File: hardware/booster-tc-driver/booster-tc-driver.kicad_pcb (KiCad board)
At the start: 2 copper layers, 53.5 x 89 mm, 42 parts, among them J1 62201021121, J2 EHT-105-01-S-D, Q1 T2N7002AK, U1 STM32F405RGTx, U2 LT1963AxST-3.3, U4 IF-D95T << must be T, U6 IF-D95T << must be T

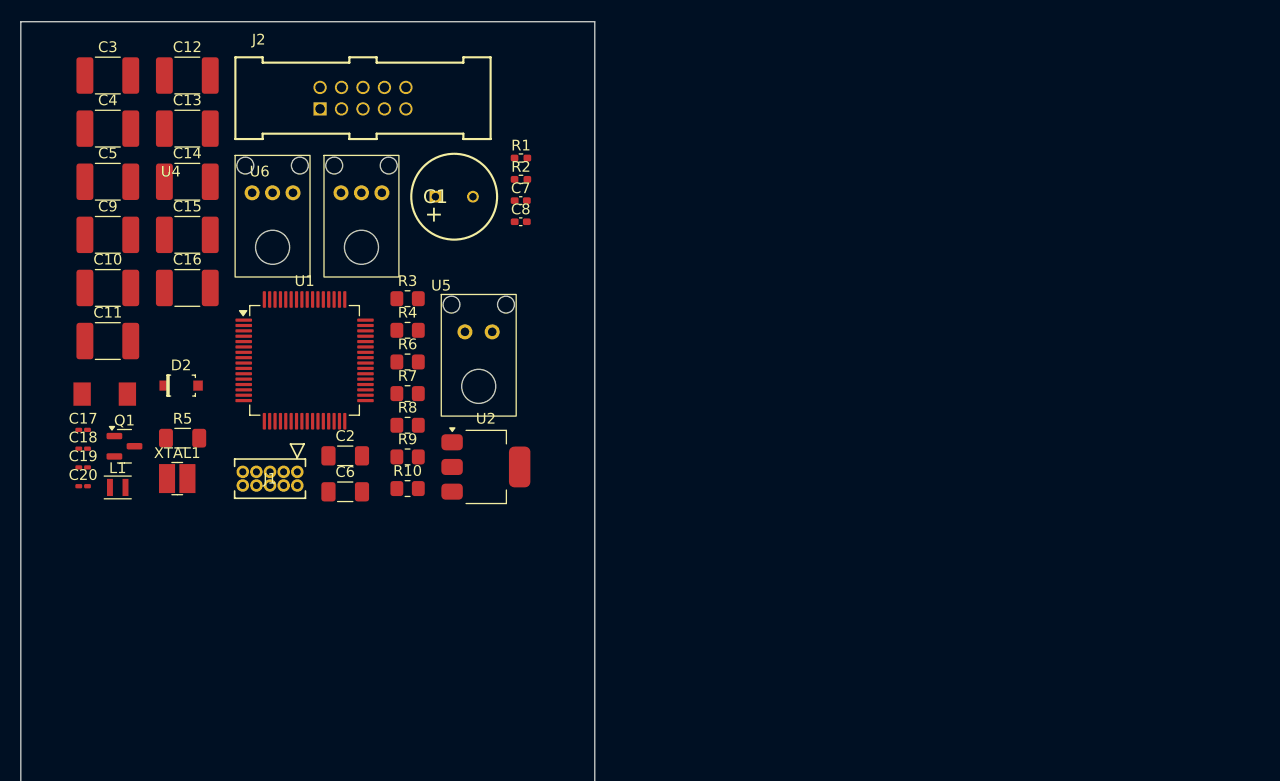
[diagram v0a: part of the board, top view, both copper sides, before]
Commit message: pin assignments
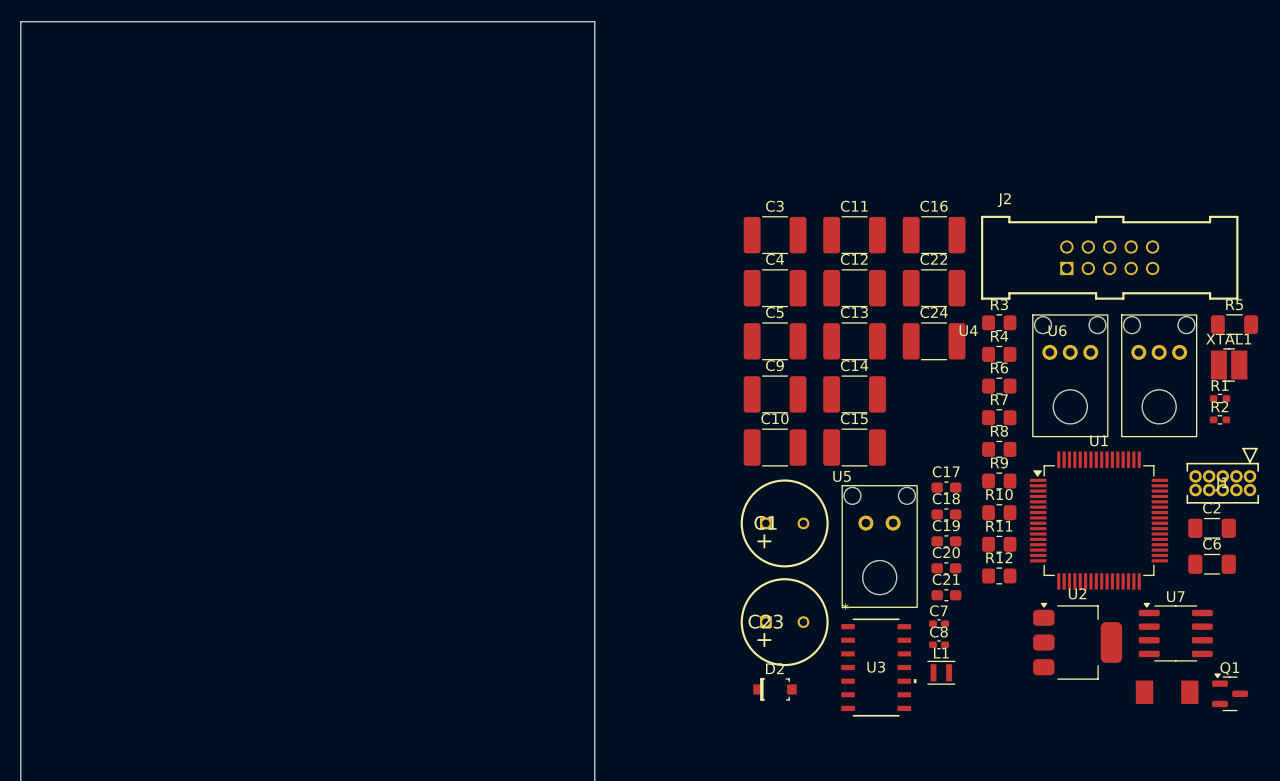
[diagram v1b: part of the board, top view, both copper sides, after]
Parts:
- added C21: 1n CGA3EAC0G2A102J080AA, Capacitor_SMD:C_0603_1608Metric_Pad1.08x0.95mm_HandSolder, F.Cu at (160.8, 112.5)
- added C22: 1u 885012210031, Capacitor_SMD:C_1812_4532Metric_Pad1.57x3.40mm_HandSolder, F.Cu at (159.6, 83.8)
- added C23: 860020474014, Library:CAPPRD350W52D800H1300, F.Cu at (143.9, 115.0)
- added C24: 1u 885012210031, Capacitor_SMD:C_1812_4532Metric_Pad1.57x3.40mm_HandSolder, F.Cu at (159.6, 88.8)
- added R11: 1k MCU0805MD1051BP500, Resistor_SMD:R_0805_2012Metric_Pad1.20x1.40mm_HandSolder, F.Cu at (165.7, 107.7)
- added R12: 1k MCU0805MD1051BP500, Resistor_SMD:R_0805_2012Metric_Pad1.20x1.40mm_HandSolder, F.Cu at (165.7, 110.7)
- added U3: MAX9202ESD+, Library:21-0041B_14-L, F.Cu at (154.2, 119.2)
- added U7: TC7662Bx0A, Package_SO:SOIC-8_3.9x4.9mm_P1.27mm, F.Cu at (182.2, 116.0)
- C17, C18, C19, C20: footprint Capacitor_SMD:C_0201_0603Metric_Pad0.64x0.40mm_HandSolder -> Capacitor_SMD:C_0603_1608Metric_Pad1.08x0.95mm_HandSolder
- moved Q1 105.6 mm to (187.2, 121.6)
- moved D1 102.9 mm to (181.4, 121.5)
- moved R5 98.6 mm to (187.6, 87.2)
- moved XTAL1 98.6 mm to (187.1, 91.0)
- moved J1 88.8 mm to (189.1, 101.4)
- moved C2 81.1 mm to (185.5, 106.2)
- moved C6 81.1 mm to (185.5, 109.6)
- moved C20 80.8 mm to (160.8, 110.0)
- moved C19 80.8 mm to (160.8, 107.4)
- moved C18 80.7 mm to (160.8, 104.9)
- moved C17 80.6 mm to (160.8, 102.4)
- moved L1 78.7 mm to (160.3, 119.7)
- moved U4 75.8 mm to (168.8, 86.3)
- moved U6 75.8 mm to (177.1, 86.3)
- moved U1 75.5 mm to (175.0, 105.5)
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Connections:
- net Net-(J2-Pad10) renamed /VAC_IN
- U1 pad 10: unconnected-(U1-PC2-Pad10) -> /I_COMP
- U1 pad 11: unconnected-(U1-PC3-Pad11) -> /I_PRI
- U1 pad 14: unconnected-(U1-PA0-Pad14) -> /VBUS_SENSE
- U1 pad 15: unconnected-(U1-PA1-Pad15) -> /THERM1
- U1 pad 16: unconnected-(U1-PA2-Pad16) -> /THERM2
- U1 pad 17: unconnected-(U1-PA3-Pad17) -> /THERM3
- U1 pad 21: unconnected-(U1-PA5-Pad21) -> /I_L
- U1 pad 22: unconnected-(U1-PA6-Pad22) -> Net-(U1-PA6)
- U1 pad 23: /VBUS_SENSE -> unconnected-(U1-PA7-Pad23)
- U1 pad 24: /I_L -> unconnected-(U1-PC4-Pad24)
- U1 pad 26: unconnected-(U1-PB0-Pad26) -> /SCR
- U1 pad 27: /SCR -> unconnected-(U1-PB1-Pad27)
- U1 pad 29: /PFC -> unconnected-(U1-PB10-Pad29)
- U1 pad 35: unconnected-(U1-PB14-Pad35) -> /FAN_1
- U1 pad 36: unconnected-(U1-PB15-Pad36) -> /FAN_2
- U1 pad 37: unconnected-(U1-PC6-Pad37) -> /LED_IDRAW
- U1 pad 39: unconnected-(U1-PC8-Pad39) -> /LED_TEMP
- U1 pad 40: unconnected-(U1-PC9-Pad40) -> /VAC_TRIG
- U1 pad 41: unconnected-(U1-PA8-Pad41) -> /PFC
- U1 pad 58: unconnected-(U1-PB6-Pad58) -> /RGB_1
- U1 pad 59: unconnected-(U1-PB7-Pad59) -> /RGB_2
- U1 pad 61: unconnected-(U1-PB8-Pad61) -> /RGB_3

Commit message: driver pcb
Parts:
- removed L1: 4u7 LQM2MPN4R7NG0L, Inductor_SMD:L_Murata_DFE201610P
- removed XTAL1: NX3225GD-8MHZ-STD-CRA-3, digikey-footprints:SMD-2_3.2x2.5mm
- added C25: 1n CGA3EAC0G2A102J080AA, Capacitor_SMD:C_0603_1608Metric_Pad1.08x0.95mm_HandSolder, F.Cu at (33.5, 64.2)
- added C26: .1uf 885012208087, Capacitor_SMD:C_1206_3216Metric_Pad1.33x1.80mm_HandSolder, F.Cu at (39.2, 42.2)
- added C27: .1uf 885012208087, Capacitor_SMD:C_1206_3216Metric_Pad1.33x1.80mm_HandSolder, B.Cu at (55.8, 50.0)
- added C28: .1uf 885012208087, Capacitor_SMD:C_1206_3216Metric_Pad1.33x1.80mm_HandSolder, B.Cu at (58.8, 42.0)
- added C29: 2u2 C3225X7R1H225K250AB, Capacitor_SMD:C_1210_3225Metric_Pad1.33x2.70mm_HandSolder, B.Cu at (63.2, 37.5)
- added C30: 22n VJ0805Y223KBBBE31, Capacitor_SMD:C_0805_2012Metric_Pad1.18x1.45mm_HandSolder, B.Cu at (55.0, 46.8)
- added C31: 1n CGA3EAC0G2A102J080AA, Capacitor_SMD:C_0603_1608Metric_Pad1.08x0.95mm_HandSolder, B.Cu at (52.4, 42.2)
- added C32: .1uf 885012208087, Capacitor_SMD:C_1206_3216Metric_Pad1.33x1.80mm_HandSolder, B.Cu at (35.0, 66.0)
- added C33: .1uf 885012208087, Capacitor_SMD:C_1206_3216Metric_Pad1.33x1.80mm_HandSolder, B.Cu at (37.5, 66.0)
- added C34: 2u2 C3225X7R1H225K250AB, Capacitor_SMD:C_1210_3225Metric_Pad1.33x2.70mm_HandSolder, F.Cu at (56.5, 79.2)
- added C35: .1uf 885012208087, Capacitor_SMD:C_1206_3216Metric_Pad1.33x1.80mm_HandSolder, F.Cu at (53.2, 75.5)
- added C36: .1uf 885012208087, Capacitor_SMD:C_1206_3216Metric_Pad1.33x1.80mm_HandSolder, F.Cu at (28.2, 46.8)
- added C37: 1n CGA3EAC0G2A102J080AA, Capacitor_SMD:C_0603_1608Metric_Pad1.08x0.95mm_HandSolder, B.Cu at (22.0, 34.0)
- added C38: .1uf C0603C104K3RECTU, Capacitor_SMD:C_0603_1608Metric_Pad1.08x0.95mm_HandSolder, B.Cu at (49.5, 68.5)
- added C39: 22n VJ0805Y223KBBBE31, Capacitor_SMD:C_0805_2012Metric_Pad1.18x1.45mm_HandSolder, B.Cu at (24.0, 37.7)
- added C40: .1uf 885012208087, Capacitor_SMD:C_1206_3216Metric_Pad1.33x1.80mm_HandSolder, B.Cu at (30.0, 31.0)
- added C41: .1uf 885012208087, Capacitor_SMD:C_1206_3216Metric_Pad1.33x1.80mm_HandSolder, B.Cu at (25.5, 34.5)
- added C42: .1uf 885012208087, Capacitor_SMD:C_1206_3216Metric_Pad1.33x1.80mm_HandSolder, B.Cu at (26.5, 48.5)
- added C43: 330u 860020575013, Library:860020575013, F.Cu at (32.7, 32.5)
- added C44: .1uf 885012208087, Capacitor_SMD:C_1206_3216Metric_Pad1.33x1.80mm_HandSolder, F.Cu at (47.2, 39.5)
- added C45: 330u 860020575013, Library:860020575013, F.Cu at (28.0, 27.2)
- added C46: 2u2 C3225X7R1H225K250AB, Capacitor_SMD:C_1210_3225Metric_Pad1.33x2.70mm_HandSolder, B.Cu at (38.8, 53.0)
- added C47: 2u2 C3225X7R1H225K250AB, Capacitor_SMD:C_1210_3225Metric_Pad1.33x2.70mm_HandSolder, B.Cu at (52.8, 37.5)
- added C48: 2u2 C3225X7R1H225K250AB, Capacitor_SMD:C_1210_3225Metric_Pad1.33x2.70mm_HandSolder, B.Cu at (56.2, 37.5)
- added C49: 2u2 C3225X7R1H225K250AB, Capacitor_SMD:C_1210_3225Metric_Pad1.33x2.70mm_HandSolder, B.Cu at (59.8, 37.5)
- added C50: .1uf C0603C104K3RECTU, Capacitor_SMD:C_0603_1608Metric_Pad1.08x0.95mm_HandSolder, F.Cu at (56.2, 71.8)
- added C51: .1uf 885012208087, Capacitor_SMD:C_1206_3216Metric_Pad1.33x1.80mm_HandSolder, B.Cu at (25.5, 24.8)
- added C52: .1uf 885012208087, Capacitor_SMD:C_1206_3216Metric_Pad1.33x1.80mm_HandSolder, B.Cu at (50.2, 33.0)
- added C53: 2u2 C3225X7R1H225K250AB, Capacitor_SMD:C_1210_3225Metric_Pad1.33x2.70mm_HandSolder, F.Cu at (62.5, 31.5)
- added C54: 2u2 C3225X7R1H225K250AB, Capacitor_SMD:C_1210_3225Metric_Pad1.33x2.70mm_HandSolder, F.Cu at (43.5, 31.5)
- added C55: 1u C1206C105K5RACTU, Capacitor_SMD:C_1206_3216Metric_Pad1.33x1.80mm_HandSolder, F.Cu at (43.5, 25.5)
- added C56: 1n CGA3EAC0G2A102J080AA, Capacitor_SMD:C_0603_1608Metric_Pad1.08x0.95mm_HandSolder, F.Cu at (60.5, 57.5)
- added C57: 22n VJ0805Y223KBBBE31, Capacitor_SMD:C_0805_2012Metric_Pad1.18x1.45mm_HandSolder, F.Cu at (63.2, 56.8)
- added C58: .1uf 885012208087, Capacitor_SMD:C_1206_3216Metric_Pad1.33x1.80mm_HandSolder, F.Cu at (57.0, 57.0)
- added C59: .1uf 885012208087, Capacitor_SMD:C_1206_3216Metric_Pad1.33x1.80mm_HandSolder, F.Cu at (62.5, 42.0)
- added C60: .1uf 885012208087, Capacitor_SMD:C_1206_3216Metric_Pad1.33x1.80mm_HandSolder, F.Cu at (56.5, 38.2)
- added C61: 1u C1206C105K5RACTU, Capacitor_SMD:C_1206_3216Metric_Pad1.33x1.80mm_HandSolder, F.Cu at (62.5, 25.2)
- added D10: MBR0530, digikey-footprints:SOD-123, B.Cu at (46.2, 73.0)
- added D11: MCL4148, Diode_SMD:D_MicroMELF, F.Cu at (37.2, 39.5)
- added D12: MCL4148, Diode_SMD:D_MicroMELF, F.Cu at (50.0, 38.0)
- added D13: SMBJ5.0A-TR, kicad-libraries-master:DO-214AA, B.Cu at (42.0, 58.2)
- added D14: PMEG4050EP, Diode_SMD:D_SOD-128, B.Cu at (45.2, 52.2)
- added D15: PMEG4050EP, Diode_SMD:D_SOD-128, B.Cu at (28.0, 44.0)
- added D16: 5700100132F, Library:LED_5700100132F, F.Cu at (61.9, 81.0)
- added D17: MCL4148, Diode_SMD:D_MicroMELF, F.Cu at (58.8, 41.2)
- added D18: MCL4148, Diode_SMD:D_MicroMELF, F.Cu at (53.0, 38.8)
- added D3: 1N5819HW-7-F, digikey-footprints:SOD-123, F.Cu at (27.8, 56.5)
- added D4: 1N5819HW-7-F, digikey-footprints:SOD-123, F.Cu at (27.8, 58.5)
- added D5: 1N5819HW-7-F, digikey-footprints:SOD-123, F.Cu at (22.8, 56.5)
- added D6: 1N5819HW-7-F, digikey-footprints:SOD-123, F.Cu at (22.8, 58.5)
- added D7: MBR0530, digikey-footprints:SOD-123, F.Cu at (23.5, 53.0)
- added D8: MBR0530, digikey-footprints:SOD-123, F.Cu at (39.5, 45.8)
- added D9: MBR0530, digikey-footprints:SOD-123, B.Cu at (46.2, 75.0)
- added IC1: AD5160BRJZ5-RL7, Library:SOT65P280X145-8N, B.Cu at (58.2, 47.0)
- added IC2: AD5160BRJZ5-RL7, Library:SOT65P280X145-8N, B.Cu at (27.0, 31.0)
- added IC3: BD50FD0WHFP-TR, Library:BD50FD0WHFPTR, B.Cu at (26.3, 56.6)
- added IC4: CAT4109V-GT2, Library:CAT4109V-GT2, B.Cu at (54.5, 80.8)
- added IC5: L4940D2T12-TR, Library:L4940D2T12-TR, B.Cu at (42.0, 25.2)
- added IC6: SI4564DY-T1-GE3, Library:SOIC127P600X175-8N, F.Cu at (43.2, 37.2)
- added IC7: SI4564DY-T1-GE3, Library:SOIC127P600X175-8N, F.Cu at (50.4, 33.2)
- added IC8: SI4564DY-T1-GE3, Library:SOIC127P600X175-8N, F.Cu at (62.5, 37.0)
- added IC9: SI4564DY-T1-GE3, Library:SOIC127P600X175-8N, F.Cu at (56.0, 33.2)
- added J10: 3-647166-2, Library:36471662, F.Cu at (25.8, 38.3)
- added J3: 3-647166-2, Library:36471662, F.Cu at (23.8, 65.0)
- added J4: 22-23-2021, digikey-footprints:PinHeader_1x2_P2.54mm_Drill1.02mm, F.Cu at (49.5, 28.0)
- added J5: 22-23-2021, digikey-footprints:PinHeader_1x2_P2.54mm_Drill1.02mm, F.Cu at (56.5, 28.0)
- added J6: 22-23-2021, digikey-footprints:PinHeader_1x2_P2.54mm_Drill1.02mm, F.Cu at (25.0, 17.8)
- added J7: 3-647166-2, Library:36471662, F.Cu at (33.0, 47.5)
- added J8: B4B-PH-SM4-TB, Library:CONN_B4B-PH-SM4-TB_JST, F.Cu at (39.0, 59.8)
- added L2: 4u7 LQM2MPN4R7NG0L, Inductor_SMD:L_Murata_DFE201610P, F.Cu at (57.2, 75.5)
- added L4: 22u 7443551221, Library:7443551221, B.Cu at (54.8, 58.2)
- added L5: 22u 7443551221, Library:7443551221, B.Cu at (36.5, 41.5)
- added R13: 1k MCU0805MD1051BP500, Resistor_SMD:R_0805_2012Metric_Pad1.20x1.40mm_HandSolder, F.Cu at (28.5, 67.5)
- added R14: 5R1 ERJ-B1BF5R1U, Resistor_SMD:R_1020_2550Metric_Pad1.33x5.20mm_HandSolder, F.Cu at (29.5, 62.5)
- added R15: 47k CRCW080547K0FKEA, Resistor_SMD:R_0805_2012Metric_Pad1.20x1.40mm_HandSolder, B.Cu at (22.0, 48.5)
- added R16: 470k CRCW0805470KFKTA, Resistor_SMD:R_0805_2012Metric_Pad1.20x1.40mm_HandSolder, B.Cu at (21.5, 37.5)
- added R17: 3k CRCW08053K00FKTA, Resistor_SMD:R_0805_2012Metric_Pad1.20x1.40mm_HandSolder, B.Cu at (24.0, 31.0)
- added R18: 82k CRCW080582K0FKEA, Resistor_SMD:R_0805_2012Metric_Pad1.20x1.40mm_HandSolder, B.Cu at (28.2, 37.8)
- added R21: 1k MCU0805MD1051BP500, Resistor_SMD:R_0805_2012Metric_Pad1.20x1.40mm_HandSolder, F.Cu at (21.5, 72.8)
- added R22: 5k CRCW06035K10FKEC, Resistor_SMD:R_0603_1608Metric_Pad0.98x0.95mm_HandSolder, F.Cu at (51.9, 55.0)
- added R23: 1k MCU0805MD1051BP500, Resistor_SMD:R_0805_2012Metric_Pad1.20x1.40mm_HandSolder, F.Cu at (39.2, 39.0)
- added R24: 1k MCU0805MD1051BP500, Resistor_SMD:R_0805_2012Metric_Pad1.20x1.40mm_HandSolder, F.Cu at (50.2, 40.0)
- added R25: 24k9 CRCW060324K9FKEA, Resistor_SMD:R_0603_1608Metric_Pad0.98x0.95mm_HandSolder, B.Cu at (50.0, 73.8)
- added R26: 24k9 CRCW060324K9FKEA, Resistor_SMD:R_0603_1608Metric_Pad0.98x0.95mm_HandSolder, B.Cu at (53.5, 73.8)
- added R27: 24k9 CRCW060324K9FKEA, Resistor_SMD:R_0603_1608Metric_Pad0.98x0.95mm_HandSolder, B.Cu at (51.8, 73.8)
- added R28: 15R CRCW121015R0JNEAHP, Resistor_SMD:R_1210_3225Metric_Pad1.30x2.65mm_HandSolder, F.Cu at (43.5, 28.2)
- added R29: 5k CRCW06035K10FKEC, Resistor_SMD:R_0603_1608Metric_Pad0.98x0.95mm_HandSolder, F.Cu at (63.2, 58.5)
- added R30: 1k MCU0805MD1051BP500, Resistor_SMD:R_0805_2012Metric_Pad1.20x1.40mm_HandSolder, F.Cu at (57.0, 41.2)
- added R31: 1k MCU0805MD1051BP500, Resistor_SMD:R_0805_2012Metric_Pad1.20x1.40mm_HandSolder, F.Cu at (54.0, 41.2)
- added R32: 15R CRCW121015R0JNEAHP, Resistor_SMD:R_1210_3225Metric_Pad1.30x2.65mm_HandSolder, F.Cu at (62.5, 28.2)
- added R33: 10k CRCW080510K0DHEAP, Resistor_SMD:R_0805_2012Metric_Pad1.20x1.40mm_HandSolder, B.Cu at (53.0, 71.0)
- added R34: 10k CRCW080510K0DHEAP, Resistor_SMD:R_0805_2012Metric_Pad1.20x1.40mm_HandSolder, B.Cu at (53.0, 68.5)
- added SW1: SW_SPDT, Library:B12JV, F.Cu at (24.5, 82.0)
- added U10: LT1963AxST-3.3, Package_TO_SOT_SMD:SOT-223-3_TabPin2, B.Cu at (25.2, 67.2)
- added U8: UCC21520DW, Package_SO:SOIC-16W_7.5x10.3mm_P1.27mm, F.Cu at (47.6, 48.2)
- added U9: UCC21520DW, Package_SO:SOIC-16W_7.5x10.3mm_P1.27mm, F.Cu at (59.1, 49.6)
- C1: value 860020474014 -> 1n CGA3EAC0G2A102J080AA; footprint Library:CAPPRD350W52D800H1300 -> Capacitor_SMD:C_0603_1608Metric_Pad1.08x0.95mm_HandSolder
- C10, C13: value 1u 885012210031 -> .1uf C0603C104K3RECTU; footprint Capacitor_SMD:C_1812_4532Metric_Pad1.57x3.40mm_HandSolder -> Capacitor_SMD:C_0603_1608Metric_Pad1.08x0.95mm_HandSolder; moved to B.Cu
- C11, C12, C9: value 1u 885012210031 -> .1uf C0603C104K3RECTU; footprint Capacitor_SMD:C_1812_4532Metric_Pad1.57x3.40mm_HandSolder -> Capacitor_SMD:C_0603_1608Metric_Pad1.08x0.95mm_HandSolder
- C14: value 1u 885012210031 -> 1n CGA3EAC0G2A102J080AA; footprint Capacitor_SMD:C_1812_4532Metric_Pad1.57x3.40mm_HandSolder -> Capacitor_SMD:C_0603_1608Metric_Pad1.08x0.95mm_HandSolder
- C15, C16: value 1u 885012210031 -> 2u2 C3225X7R1H225K250AB; footprint Capacitor_SMD:C_1812_4532Metric_Pad1.57x3.40mm_HandSolder -> Capacitor_SMD:C_1210_3225Metric_Pad1.33x2.70mm_HandSolder
- C18: value 1n CGA3EAC0G2A102J080AA -> .1uf 885012208087; footprint Capacitor_SMD:C_0603_1608Metric_Pad1.08x0.95mm_HandSolder -> Capacitor_SMD:C_1206_3216Metric_Pad1.33x1.80mm_HandSolder
- C2: value .1uf 885012208087 -> 2u2 C3225X7R1H225K250AB; footprint Capacitor_SMD:C_1206_3216Metric_Pad1.33x1.80mm_HandSolder -> Capacitor_SMD:C_1210_3225Metric_Pad1.33x2.70mm_HandSolder; moved to B.Cu
- C20: value 1n CGA3EAC0G2A102J080AA -> 2u2 C3225X7R1H225K250AB; footprint Capacitor_SMD:C_0603_1608Metric_Pad1.08x0.95mm_HandSolder -> Capacitor_SMD:C_1210_3225Metric_Pad1.33x2.70mm_HandSolder; moved to B.Cu
- C21: value 1n CGA3EAC0G2A102J080AA -> 330u 860020575013; footprint Capacitor_SMD:C_0603_1608Metric_Pad1.08x0.95mm_HandSolder -> Library:860020575013
- C22, C24: value 1u 885012210031 -> .1uf 885012208087; footprint Capacitor_SMD:C_1812_4532Metric_Pad1.57x3.40mm_HandSolder -> Capacitor_SMD:C_1206_3216Metric_Pad1.33x1.80mm_HandSolder; moved to B.Cu
- C23: value 860020474014 -> .1uf 885012208087; footprint Library:CAPPRD350W52D800H1300 -> Capacitor_SMD:C_1206_3216Metric_Pad1.33x1.80mm_HandSolder; moved to B.Cu
- C3: value 1u 885012210031 -> 330u 860020575013; footprint Capacitor_SMD:C_1812_4532Metric_Pad1.57x3.40mm_HandSolder -> Library:860020575013
- C4: value 1u 885012210031 -> 22n VJ0805Y223KBBBE31; footprint Capacitor_SMD:C_1812_4532Metric_Pad1.57x3.40mm_HandSolder -> Capacitor_SMD:C_0805_2012Metric_Pad1.18x1.45mm_HandSolder
- C5: value 1u 885012210031 -> 2u2 C3225X7R1H225K250AB; footprint Capacitor_SMD:C_1812_4532Metric_Pad1.57x3.40mm_HandSolder -> Capacitor_SMD:C_1210_3225Metric_Pad1.33x2.70mm_HandSolder; moved to B.Cu
- C6, R7, R9: moved to B.Cu
- C7: value 16p 04025U160FAT2A -> 1n CGA3EAC0G2A102J080AA; footprint Capacitor_SMD:C_0402_1005Metric_Pad0.74x0.62mm_HandSolder -> Capacitor_SMD:C_0603_1608Metric_Pad1.08x0.95mm_HandSolder; moved to B.Cu
- C8: value 16p 04025U160FAT2A -> 1u C1206C105K5RACTU; footprint Capacitor_SMD:C_0402_1005Metric_Pad0.74x0.62mm_HandSolder -> Capacitor_SMD:C_1206_3216Metric_Pad1.33x1.80mm_HandSolder; moved to B.Cu
- D1: value SMBJ5.0A-TR -> SMBJ3V3; moved to B.Cu
- D2: value 1N5819HW-7-F -> MBR0530
- R1: value 10k ESR01MZPF1002 -> 3k CRCW08053K00FKTA; footprint Resistor_SMD:R_0402_1005Metric_Pad0.72x0.64mm_HandSolder -> Resistor_SMD:R_0805_2012Metric_Pad1.20x1.40mm_HandSolder; moved to B.Cu
- R11: value 1k MCU0805MD1051BP500 -> 47k CRCW080547K0FKEA; moved to B.Cu
- R12: value 1k MCU0805MD1051BP500 -> 470k CRCW0805470KFKTA; moved to B.Cu
- R2: value 10k ESR01MZPF1002 -> 82k CRCW080582K0FKEA; footprint Resistor_SMD:R_0402_1005Metric_Pad0.72x0.64mm_HandSolder -> Resistor_SMD:R_0805_2012Metric_Pad1.20x1.40mm_HandSolder; moved to B.Cu
- U1: value STM32F405RGTx -> STM32G474CBTx; footprint Package_QFP:LQFP-64_10x10mm_P0.5mm -> Package_QFP:LQFP-48_7x7mm_P0.5mm
- U2: value LT1963AxST-3.3 -> AOZ1284PI; footprint Package_TO_SOT_SMD:SOT-223-3_TabPin2 -> Package_SO:SOIC-8-1EP_3.9x4.9mm_P1.27mm_EP2.29x3mm; moved to B.Cu
- U3: value MAX9202ESD+ -> CSTNE8M00G550000R0; footprint Library:21-0041B_14-L -> Library:CSTNE16M0V530000R0
- U5: value ~ -> IF-E96E
- U7: value TC7662Bx0A -> AOZ1284PI; footprint Package_SO:SOIC-8_3.9x4.9mm_P1.27mm -> Package_SO:SOIC-8-1EP_3.9x4.9mm_P1.27mm_EP2.29x3mm; moved to B.Cu
- moved U7 174.3 mm to (23.6, 43.5), turned to 90 degrees
- moved C2 159.9 mm to (34.8, 53.0), turned to 90 degrees
- moved D1 158.8 mm to (32.2, 66.8), turned to -90 degrees
- moved C6 154.8 mm to (41.8, 52.2), turned to 90 degrees
- moved C21 153.8 mm to (35.0, 24.0), turned to 90 degrees
- moved R8 153.2 mm to (22.0, 45.8)
- moved C19 150.9 mm to (22.2, 47.5), turned to 180 degrees
- moved R10 146.8 mm to (34.0, 40.0), turned to 90 degrees
- moved U2 141.7 mm to (50.3, 46.0)
- moved U6 141.5 mm to (35.6, 88.1), turned to 180 degrees
- moved D2 141.1 mm to (21.2, 53.0), turned to -90 degrees
- moved Q1 140.8 mm to (52.5, 80.7), turned to -90 degrees
- moved R6 137.9 mm to (29.0, 74.8), turned to -90 degrees
- moved J2 137.3 mm to (53.0, 20.0)
- moved R1 137.2 mm to (58.5, 44.2), turned to 180 degrees
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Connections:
- net Net-(J2-Pad01) renamed /I_L_IN
- net Net-(J2-Pad08) renamed /VBUS_IN
- C1 pad 1: +5V -> Net-(C1-Pad1)
- C10 pad 1: VDD -> GND
- C10 pad 2: GND -> /VREF
- C13 pad 1: /VCAP1 -> /THERM2
- C14 pad 1: /VCAP2 -> GND
- C14 pad 2: GND -> GDT1_DIS
- C18 pad 1: /VAC_SENSE -> GND
- C18 pad 2: GND -> +12V
- C20 pad 1: /PFC -> +5V
- C21 pad 1: GND -> +24V
- C21 pad 2: Net-(U1-PA6) -> GND
- C22 pad 1: Net-(U7-CAP+) -> GND
- C22 pad 2: Net-(U7-CAP-) -> +5V
- C23 pad 1: GND -> Net-(U2-BST)
- C23 pad 2: -5V -> Net-(D14-K)
- C24 pad 2: -5V -> +24V
- C4 pad 1: VDD -> Net-(U8-DT)
- C5 pad 1: VDDA -> +5V
- C6 pad 1: VDDA -> +5V
- C7 pad 1: GND -> /VAC_SENSE
- C7 pad 2: Net-(U1-PH0) -> GND
- C8 pad 2: Net-(U1-PH1) -> /VREF
- D1 pad 1: +5V -> VDD
- J2 pad 04: Net-(J2-Pad04) -> /PFC
- R1 pad 1: /BOOT0 -> Net-(IC1-A)
- R1 pad 2: GND -> Net-(U2-FB)
- R11 pad 1: /VAC_IN -> GND
- R11 pad 2: Net-(U1-PA6) -> Net-(U2-FSW)
- R12 pad 1: Net-(U1-PA6) -> Net-(C31-Pad2)
- R12 pad 2: +5V -> Net-(U2-COMP)
- R2 pad 1: /BOOT1 -> /VFAN_OUT
- R2 pad 2: GND -> Net-(U2-FB)
- R7 pad 1: Net-(J2-Pad04) -> /VAC_SENSE
- R7 pad 2: /PFC -> /VAC_IN
- R9 pad 1: /VAC_IN -> /VREF
- U1 pad 10: /I_COMP -> unconnected-(U1-PA2-Pad10)
- U1 pad 11: /I_PRI -> unconnected-(U1-PA3-Pad11)
- U1 pad 12: GND -> unconnected-(U1-PA4-Pad12)
- U1 pad 13: VDDA -> unconnected-(U1-PA5-Pad13)
- U1 pad 14: /VBUS_SENSE -> unconnected-(U1-PA6-Pad14)
- U1 pad 15: /THERM1 -> unconnected-(U1-PA7-Pad15)
- U1 pad 16: /THERM2 -> unconnected-(U1-PB0-Pad16)
- U1 pad 17: /THERM3 -> unconnected-(U1-PB1-Pad17)
- U1 pad 18: GND -> unconnected-(U1-PB2-Pad18)
- U1 pad 19: VDD -> GND
- U1 pad 20: unconnected-(U1-PA4-Pad20) -> /VREF
- U1 pad 21: /I_L -> VDDA
- U1 pad 22: Net-(U1-PA6) -> unconnected-(U1-PB10-Pad22)
- U1 pad 23: unconnected-(U1-PA7-Pad23) -> GND
- U1 pad 24: unconnected-(U1-PC4-Pad24) -> VDD
- U1 pad 26: /SCR -> unconnected-(U1-PB12-Pad26)
- U1 pad 28: /BOOT1 -> unconnected-(U1-PB14-Pad28)
- U1 pad 31: /VCAP1 -> unconnected-(U1-PA9-Pad31)
- U1 pad 32: VDD -> unconnected-(U1-PA10-Pad32)
- U1 pad 35: /FAN_1 -> GND
- U1 pad 36: /FAN_2 -> VDD
- U1 pad 37: /LED_IDRAW -> /TMS
- U1 pad 38: unconnected-(U1-PC7-Pad38) -> /TCK
- U1 pad 39: /LED_TEMP -> /TDI
- U1 pad 40: /VAC_TRIG -> /TDO
- U1 pad 41: /PFC -> unconnected-(U1-PB4-Pad41)
- U1 pad 46: /TMS -> unconnected-(U1-PB9-Pad46)
- U1 pad 47: /VCAP2 -> GND
- U1 pad 5: Net-(U1-PH0) -> Net-(U1-PF0)
- U1 pad 6: Net-(U1-PH1) -> Net-(U1-PF1)
- U1 pad 8: /INT -> unconnected-(U1-PA0-Pad8)
- U2 pad 1: +5V -> Net-(D14-K)
- U2 pad 2: GND -> Net-(U2-BST)
- U2 pad 3: VDD -> GND
- U3 pad 1: GND -> Net-(U1-PF1)
- U3 pad 2: /VAC_SENSE -> GND
- U3 pad 3: GND -> Net-(U1-PF0)
- U5 pad 2: unconnected-(U5-A-Pad2) -> +5V
- U7 pad 1: +5V -> Net-(D15-K)
- U7 pad 2: Net-(U7-CAP+) -> Net-(U7-BST)
- U7 pad 4: Net-(U7-CAP-) -> Net-(U7-FSW)
- U7 pad 5: -5V -> Net-(U7-COMP)
- U7 pad 6: unconnected-(U7-LV-Pad6) -> Net-(U7-FB)
- U7 pad 7: unconnected-(U7-OSC-Pad7) -> Net-(U7-SS)
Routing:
- net GND: track 0.00 -> 266.7 mm, vias 0 -> 102
- net +5V: track 0.00 -> 260.7 mm, vias 0 -> 5
- net +12V: track 0.00 -> 125.4 mm, vias 0 -> 1
- net /SPI_MOSI: track 0.00 -> 105.6 mm, vias 0 -> 1
- net /CS_DRIVE: track 0.00 -> 97.6 mm, vias 0 -> 1
- net /SPI_CLK: track 0.00 -> 96.4 mm, vias 0 -> 1
- net VDRIVE: track 0.00 -> 93.5 mm
- net /VAC_IN: track 0.00 -> 89.1 mm, vias 0 -> 1
- net /VBUS_IN: track 0.00 -> 57.9 mm
- net /VFAN_OUT: track 0.00 -> 57.2 mm, vias 0 -> 1
- net /SCR: track 0.00 -> 48.7 mm
- net /PFC: track 0.00 -> 45.7 mm
- net /I_L_IN: track 0.00 -> 39.8 mm
- net +24V: track 0.00 -> 34.8 mm, vias 0 -> 9
- net /I_L: track 0.00 -> 28.9 mm
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- added copper zone on B.Cu, net +24V
- added copper zone on In2.Cu, net +24V
- added copper zone on B.Cu, net +5V
- added copper zone on B.Cu, net GND
- added copper zone on F.Cu, net GND
- added copper zone on In1.Cu, net GND
- added copper zone on B.Cu, net VDD
- added copper zone on In2.Cu, net VDD
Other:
- board size 53.5 x 89 mm -> 53.3 x 72 mm
- copper layers 2 -> 4

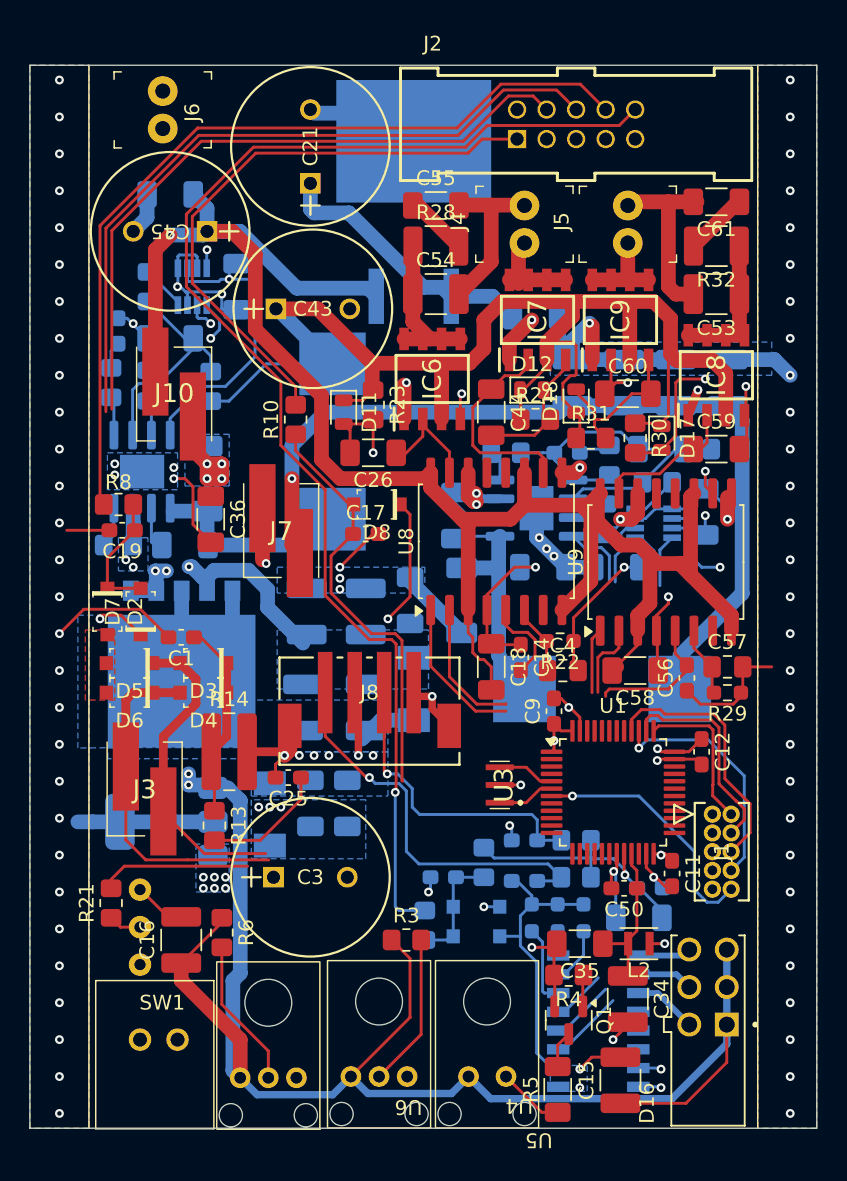
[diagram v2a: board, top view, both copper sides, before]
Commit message: driver board+code
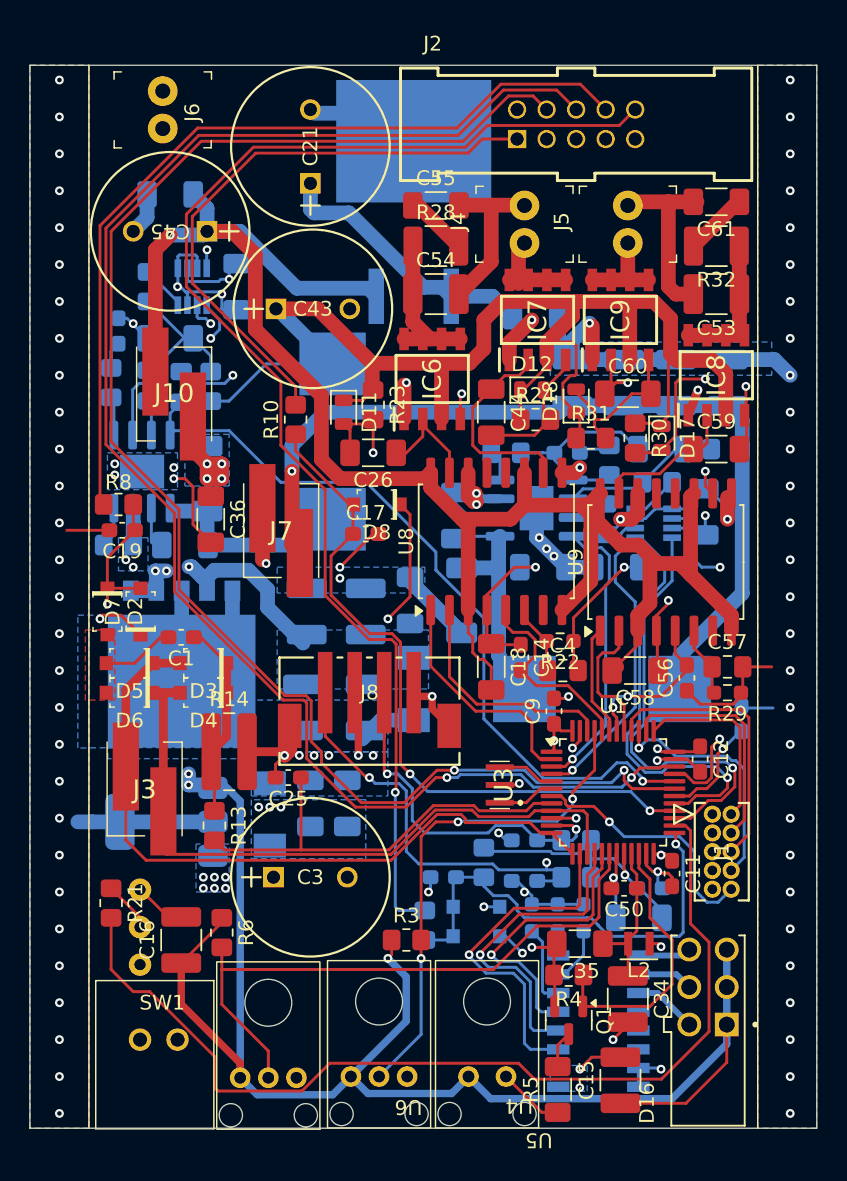
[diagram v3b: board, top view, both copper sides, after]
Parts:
- added C62: 22n VJ0805Y223KBBBE31, Capacitor_SMD:C_0805_2012Metric_Pad1.18x1.45mm_HandSolder, B.Cu at (26.2, 37.8)
- added C63: 10n VJ0603Y103KXJAC31X, Capacitor_SMD:C_0603_1608Metric_Pad1.08x0.95mm_HandSolder, B.Cu at (64.2, 60.3)
- C7: value 1n CGA3EAC0G2A102J080AA -> 10n VJ0603Y103KXJAC31X
- moved C12 0.51 mm to (61.4, 63.0)
- turned R21 to -90 degrees
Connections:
- J3 pad 1: /CT- -> /CT+
- J3 pad 2: /CT+ -> /CT-
- U1 pad 10: unconnected-(U1-PA2-Pad10) -> /THERM2
- U1 pad 11: unconnected-(U1-PA3-Pad11) -> /THERM1
- U1 pad 12: unconnected-(U1-PA4-Pad12) -> /CT-
- U1 pad 13: unconnected-(U1-PA5-Pad13) -> /CT-
- U1 pad 14: unconnected-(U1-PA6-Pad14) -> /LED_VBUS
- U1 pad 15: unconnected-(U1-PA7-Pad15) -> /CT+
- U1 pad 16: unconnected-(U1-PB0-Pad16) -> /LED_TMP
- U1 pad 17: unconnected-(U1-PB1-Pad17) -> /LED_I_IN
- U1 pad 18: unconnected-(U1-PB2-Pad18) -> /INT
- U1 pad 2: unconnected-(U1-PC13-Pad2) -> GDT1_INA
- U1 pad 22: unconnected-(U1-PB10-Pad22) -> /USART_TX
- U1 pad 25: unconnected-(U1-PB11-Pad25) -> /VAC_SENSE
- U1 pad 26: unconnected-(U1-PB12-Pad26) -> /MODE_IN
- U1 pad 27: unconnected-(U1-PB13-Pad27) -> /SPI_CLK
- U1 pad 28: unconnected-(U1-PB14-Pad28) -> /I_L
- U1 pad 29: unconnected-(U1-PB15-Pad29) -> /SPI_MOSI
- U1 pad 3: unconnected-(U1-PC14-Pad3) -> /FAN_EN
- U1 pad 30: unconnected-(U1-PA8-Pad30) -> /VBUS_SENSE
- U1 pad 31: unconnected-(U1-PA9-Pad31) -> /PFC
- U1 pad 32: unconnected-(U1-PA10-Pad32) -> /DRIVE_EN
- U1 pad 33: unconnected-(U1-PA11-Pad33) -> /CS_DRIVE
- U1 pad 34: unconnected-(U1-PA12-Pad34) -> /SCR
- U1 pad 4: unconnected-(U1-PC15-Pad4) -> /CS_FAN
- U1 pad 41: unconnected-(U1-PB4-Pad41) -> GDT2_INB
- U1 pad 42: unconnected-(U1-PB5-Pad42) -> GDT2_DIS
- U1 pad 43: unconnected-(U1-PB6-Pad43) -> GDT2_INA
- U1 pad 44: unconnected-(U1-PB7-Pad44) -> GDT1_DIS
- U1 pad 45: unconnected-(U1-PB8-Pad45) -> /USART_RX
- U1 pad 46: unconnected-(U1-PB9-Pad46) -> GDT1_INB
- U1 pad 8: unconnected-(U1-PA0-Pad8) -> /I_PRI
- U1 pad 9: unconnected-(U1-PA1-Pad9) -> /CT+
- U7 pad 8: +5V -> /DRIVE_EN
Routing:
- net /VBUS_SENSE: track 8.74 -> 119.8 mm, vias 0 -> 2
- net /SPI_CLK: track 96.4 -> 164.2 mm, vias 1 -> 2
- net /SPI_MOSI: track 105.6 -> 172.2 mm, vias 1 -> 2
- net /PFC: track 45.7 -> 104.2 mm, vias 0 -> 2
- net /SCR: track 48.7 -> 106.8 mm, vias 0 -> 2
- net /MODE_IN: track 10.2 -> 66.6 mm
- net /DRIVE_EN: track 0.00 -> 52.4 mm, vias 0 -> 1
- net /CS_DRIVE: track 97.6 -> 148.1 mm, vias 1 -> 2
- net /INT: track 10.1 -> 41.7 mm
- net /CT-: track 21.4 -> 47.9 mm
- net /CT+: track 23.6 -> 49.2 mm
- net /USART_RX: track 10.4 -> 34.2 mm, vias 0 -> 3
- net /VAC_SENSE: track 7.99 -> 30.8 mm, vias 0 -> 1
- net /I_PRI: track 8.49 -> 29.6 mm
- net /I_L: track 28.9 -> 48.2 mm, vias 0 -> 2
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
